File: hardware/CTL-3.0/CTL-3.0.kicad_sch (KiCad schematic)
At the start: 63 parts, among them J1 Conn_02x16_Top_Bottom, J2 Conn_02x05_Odd_Even, J3 Conn_01x03, J4 Conn_01x02, J5 Conn_02x06_Odd_Even, J6 Conn_01x04, J7 Conn_01x04, J8 Conn_01x04, K1 G5V-1, Q1 BCX56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

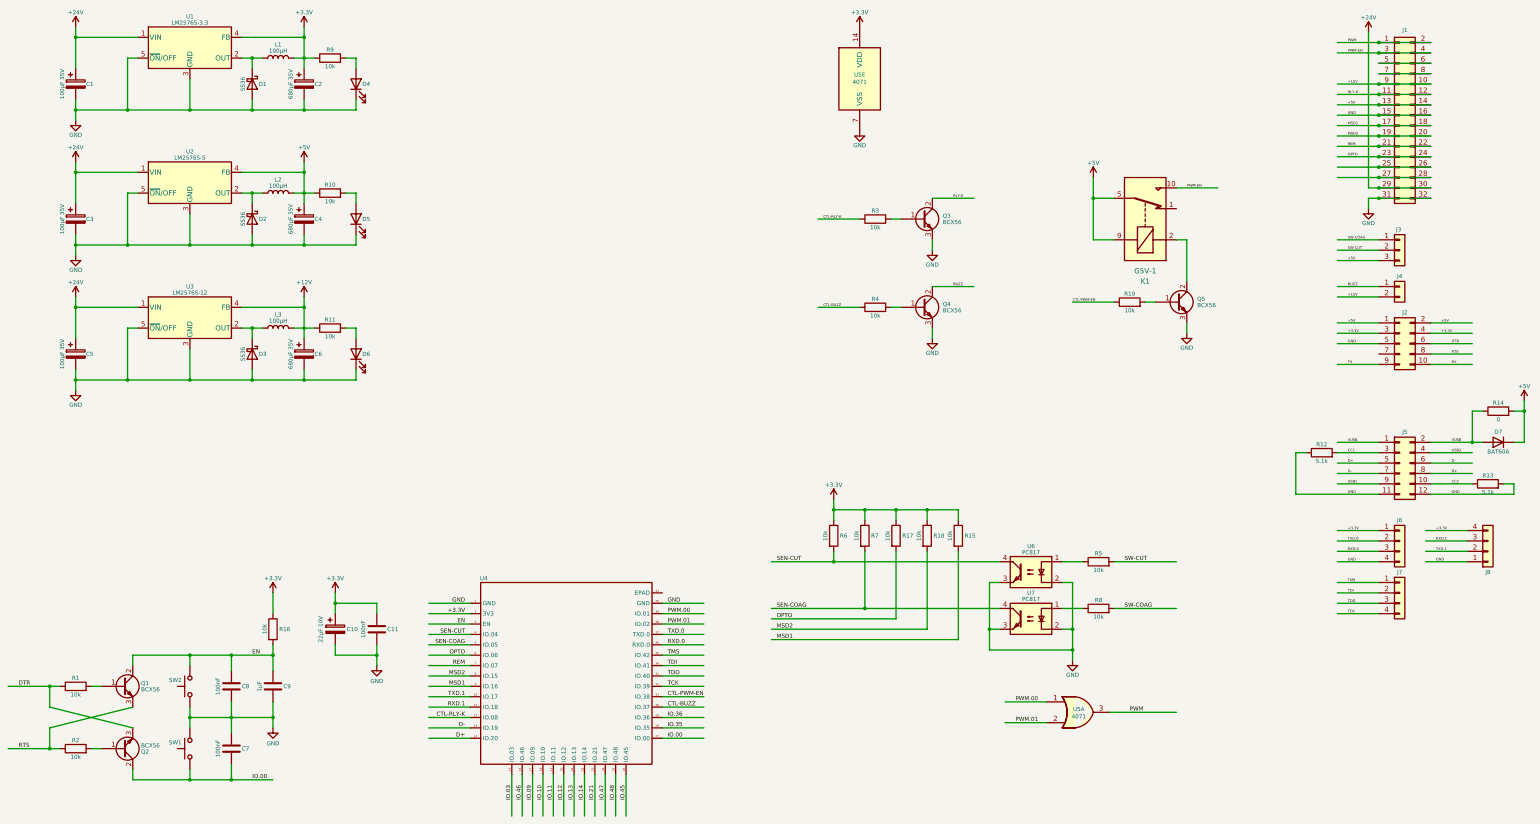
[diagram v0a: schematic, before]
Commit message: modified:   .DS_Store 	deleted:    hardware/CTL-2.0/CTL-1.0-backups/CTL-1.0-2025-06-05_145506.zip 	deleted:    hardware/CTL-2.0/CTL-1.0-backups/CTL-1.0-2025-06-10_100335.zip 	deleted:    hardware/CTL-2.0/CTL-1.0-backups/CTL-1.0-2025-06-12_095314.zip 	deleted:    hardware/CTL-2.0/CTL-1.0-backups/CTL-1.0-2025-07-03_115731.zip 	deleted:    hardware/CTL-2.0/CTL-1.0-backups/CTL-1.0-2025-07-16_143147.zip 	deleted:    hardware/CTL-2.0/CTL-1.0-backups/CTL-1.0-2025-07-24_151142.zip 	deleted:    hardware/CTL-2.0/CTL-1.0-backups/CTL-1.0-2025-07-24_172002.zip 	deleted:    hardware/CTL-2.0/CTL-1.0-backups/CTL-1.0-2025-07-25_175122.zip 	deleted:    hardware/CTL-2.0/CTL-1.0-backups/CTL-1.0-2025-07-26_120011.zip 	deleted:    hardware/CTL-2.0/CTL-1.0-backups/CTL-1.0-2025-07-26_120808.zip 	deleted:    hardware/CTL-2.0/CTL-1.0-backups/CTL-1.0-2025-07-28_094555.zip 	deleted:    hardware/CTL-2.0/CTL-1.0-backups/CTL-1.0-2025-07-28_104747.zip 	deleted:    hardware/CTL-2.0/CTL-1.0-backups/CTL-1.0-2025-07-28_112613.zip 	deleted:    hardware/CTL-2.0/CTL-1.0-backups/CTL-1.0-2025-07-28_114906.zip 	deleted:    hardware/CTL-2.0/CTL-1.0-backups/CTL-1.0-2025-07-28_120848.zip 	deleted:    hardware/CTL-2.0/CTL-1.0-backups/CTL-1.0-2025-07-29_085804.zip 	deleted:    hardware/CTL-2.0/CTL-1.0-backups/CTL-1.0-2025-07-29_150437.zip 	deleted:    hardware/CTL-2.0/CTL-1.0-backups/CTL-1.0-2025-07-30_093152.zip 	deleted:    hardware/CTL-2.0/CTL-1.0-backups/CTL-1.0-2025-07-31_095618.zip 	deleted:    hardware/CTL-2.0/CTL-1.0-backups/CTL-1.0-2025-08-01_111317.zip 	deleted:    hardware/CTL-2.0/CTL-1.0-backups/CTL-1.0-2025-08-01_113544.zip 	deleted:    hardware/CTL-2.0/CTL-1.0-backups/CTL-1.0-2025-08-01_114559.zip 	deleted:    hardware/CTL-2.0/CTL-1.0-backups/CTL-1.0-2025-08-01_115359.zip 	deleted:    hardware/CTL-2.0/CTL-1.0-backups/CTL-1.0-2025-08-01_115915.zip 	deleted:    hardware/CTL-2.0/CTL-1.0-backups/CTL-1.0-2025-08-01_131607.zip 	deleted:    hardware/CTL-2.0/CTL-1.2-TopSilkscreen.png 	deleted:    hardware/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
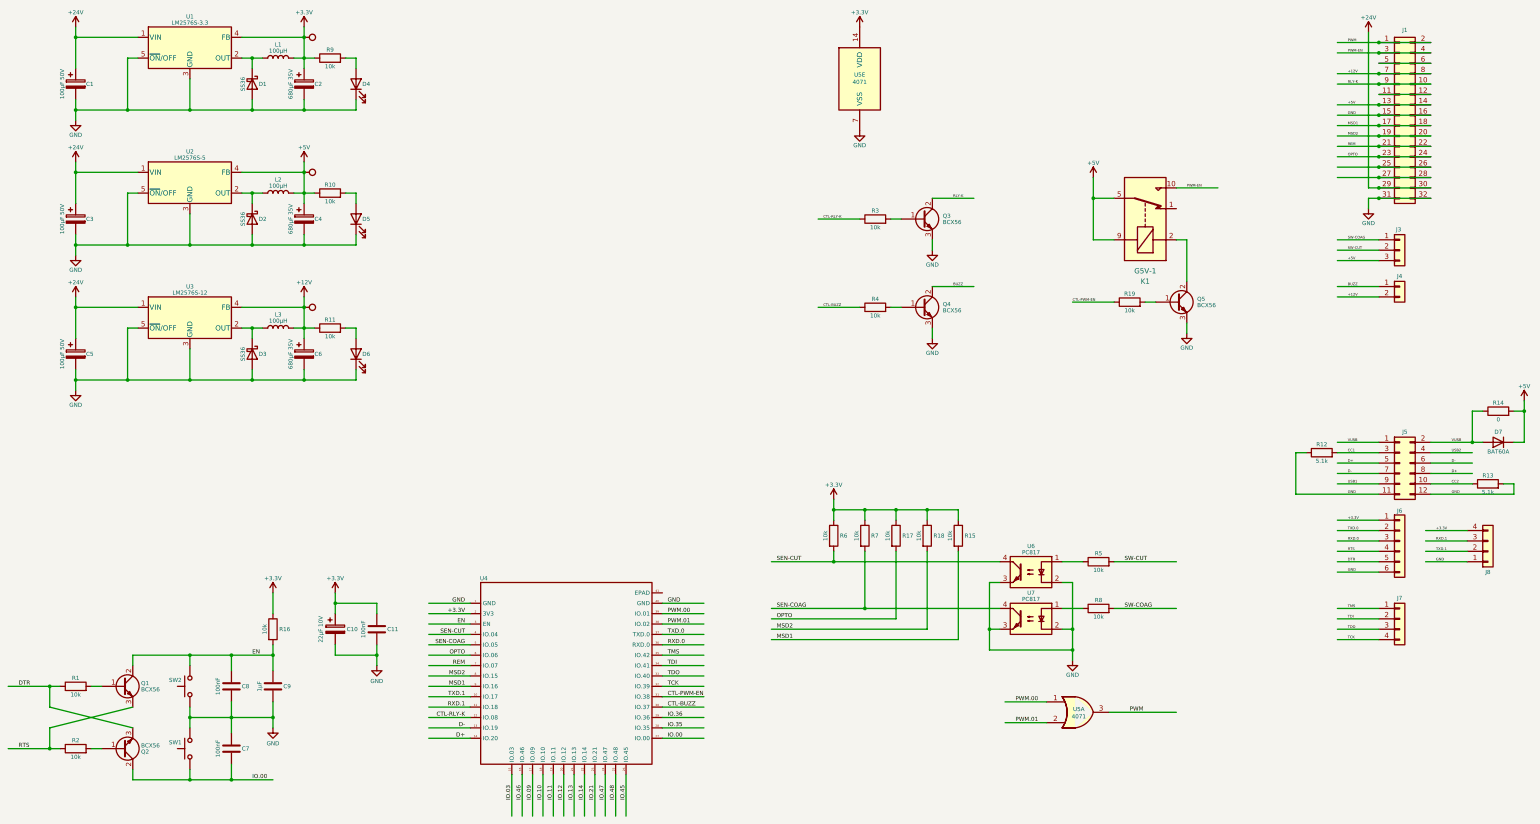
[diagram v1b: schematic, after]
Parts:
- removed J2: Conn_02x05_Odd_Even, Connector_PinHeader_2.54mm:PinHeader_2x05_P2.54mm_Vertical, symbol Connector_Generic:Conn_02x05_Odd_Even
- added TP1, TP2, TP3: TestPoint, TestPoint:TestPoint_Bridge_Pitch2.54mm_Drill1.0mm, symbol Connector:TestPoint
- C1, C3, C5: value 100µF 35V -> 100µF 50V
- J6: footprint Connector_PinHeader_2.54mm:PinHeader_1x04_P2.54mm_Vertical -> Connector_PinHeader_2.54mm:PinHeader_1x06_P2.54mm_Vertical; symbol Connector_Generic:Conn_01x04 -> Connector_Generic:Conn_01x06
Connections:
- net +12V: now also J1.7 (Pin_7), J1.8 (Pin_8), TP3.1; no longer J1.10 (Pin_10), J1.9 (Pin_9)
- net +3.3V: now also TP1.1
- net +5V: now also TP2.1
- net DTR: now also J6.5 (Pin_5)
- net GND: now also J6.6 (Pin_6); no longer J6.4 (Pin_4)
- net RLY-K: now also J1.10 (Pin_10), J1.9 (Pin_9); no longer J1.11 (Pin_11), J1.12 (Pin_12)
- net RTS: now also J6.4 (Pin_4)
- new net: J1.11 (Pin_11), J1.12 (Pin_12)
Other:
- moved on the sheet: J7

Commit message: modified:   .DS_Store 	modified:   README.md 	new file:   hardware/CTL-3.0/CTL-3.0-backups/CTL-3.0-2025-08-08_093936.zip 	new file:   hardware/CTL-3.0/CTL-3.0-backups/CTL-3.0-2025-08-08_103359.zip 	new file:   hardware/CTL-3.0/CTL-3.0-backups/CTL-3.0-2025-08-08_104842.zip 	new file:   hardware/CTL-3.0/CTL-3.0-backups/CTL-3.0-2025-08-08_105743.zip 	modified:   hardware/CTL-3.0/CTL-3.0.kicad_pcb 	modified:   hardware/CTL-3.0/CTL-3.0.kicad_sch 	modified:   hardware/CTL-3.0/CTL-3.0.step 	modified:   hardware/CTL-3.0/fp-info-cache 	modified:   hardware/MSD-1.0/MSD-1.0.step 	deleted:    hardware/PS-2.0/PS-2.0-backups/PS-2.0-2025-07-28_091511.zip 	deleted:    hardware/PS-2.0/PS-2.0-backups/PS-2.0-2025-07-28_120953.zip 	deleted:    hardware/PS-2.0/PS-2.0-backups/PS-2.0-2025-07-29_151613.zip 	deleted:    hardware/PS-2.0/PS-2.0-backups/PS-2.0-2025-07-30_104542.zip 	deleted:    hardware/PS-2.0/PS-2.0-backups/PS-2.0-2025-08-07_142024.zip 	new file:   hardware/PS-2.0/PS-2.0-backups/PS-2.0-2025-08-08_083444.zip 	new file:   hardware/PS-2.0/PS-2.0-backups/PS-2.0-2025-08-08_093021.zip 	new file:   hardware/PS-2.0/PS-2.0-backups/PS-2.0-2025-08-08_095017.zip 	new file:   hardware/PS-2.0/PS-2.0-backups/PS-2.0-2025-08-08_101231.zip 	new file:   hardware/PS-2.0/PS-2.0-backups/PS-2.0-2025-08-08_102520.zip 	modified:   hardware/PS-2.0/PS-2.0.kicad_pcb 	modified:   hardware/PS-2.0/PS-2.0.kicad_prl 	new file:   hardware/PS-2.0/~PS-2.0.kicad_pcb.lck 	modified:   hardware/REM-4.0/REM-4.0.step 	deleted:    hardware/XF-1.0/XF-1.0-backups/XF-1.0-2025-07-17_151907.zip 	deleted:    hardware/XF-1.0/XF-1.0-backups/XF-1.0-2025-08-07_145812.zip 	new file:   hardware/XF-1.0/XF-1.0-backups/XF-1.0-2025-08-08_083643.zip 	new file:   hardware/XF-1.0/XF-1.0-backups/XF-1.0-2025-08-08_100854.zip 	new file:   hardware/XF-1.0/XF-1.0-backups/XF-1.0-2025-08-08_101915.zip 	modified:   hardware/XF-1.0/XF-1.0.kicad_pcb 	modified:   hardware/XF-1.0/XF-1.0.step 	modified:   hardware/XF-1.0/fp-info-cache 	modified:   l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
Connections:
- net +12V: now also J4.1 (Pin_1); no longer J4.2 (Pin_2)
- net +5V: now also J3.1 (Pin_1); no longer J3.3 (Pin_3)
- net BUZZ: now also J4.2 (Pin_2); no longer J4.1 (Pin_1)
- net SW-COAG: now also J3.3 (Pin_3); no longer J3.1 (Pin_1)
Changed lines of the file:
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@@
 	(wire
 		(pts
-			(xy 351.79 72.39) (xy 361.95 72.39)
+			(xy 351.79 77.47) (xy 361.95 77.47)
 		)
 		(stroke
@@
 	(wire
 		(pts
-			(xy 351.79 77.47) (xy 361.95 77.47)
+			(xy 351.79 72.39) (xy 361.95 72.39)
 		)
 		(stroke
@@
 	(wire
 		(pts
-			(xy 351.79 83.82) (xy 361.95 83.82)
+			(xy 351.79 86.36) (xy 361.95 86.36)
 		)
 		(stroke
@@
 	(wire
 		(pts
-			(xy 351.79 86.36) (xy 361.95 86.36)
+			(xy 351.79 83.82) (xy 361.95 83.82)
 		)
 		(stroke
@@
 	)
 	(label "+5V"
-		(at 354.33 77.47 0)
+		(at 354.33 72.39 0)
 		(fields_autoplaced yes)
 		(effects
@@
 	)
 	(label "BUZZ"
-		(at 354.33 83.82 0)
+		(at 354.33 86.36 0)
 		(fields_autoplaced yes)
 		(effects
@@
 	)
 	(label "SW-COAG"
-		(at 354.33 72.39 0)
+		(at 354.33 77.47 0)
 		(fields_autoplaced yes)
 		(effects
@@
 	)
 	(label "+12V"
-		(at 354.33 86.36 0)
+		(at 354.33 83.82 0)
 		(fields_autoplaced yes)
 		(effects
@@
 	)
 	(symbol
+		(lib_id "Connector_Generic:Conn_01x03")
+		(at 367.03 74.93 0)
+		(unit 1)
+		(exclude_from_sim no)
+		(in_bom yes)
+		(on_board yes)
+		(dnp no)
+		(property "Reference" "J3"
+			(at 366.776 69.85 0)
+			(effects
+				(font
+					(size 1 1)
+				)
+			)
+		)
+		(property "Value" "Conn_01x03"
+			(at 369.57 76.1999 0)
+			(effects
+				(font
+					(size 1.27 1.27)
+				)
+				(justify left)
+				(hide yes)
+			)
+		)
+		(property "Footprint" "Connector_Molex:Molex_KK-396_5273-03A_1x03_P3.96mm_Vertical"
+			(at 367.03 74.93 0)
+			(effects
+				(font
+					(size 1.27 1.27)
+				)
+				(hide yes)
+			)
+		)
+		(property "Datasheet" "~"
+			(at 367.03 74.93 0)
+			(effects
+				(font
+					(size 1.27 1.27)
+				)
+				(hide yes)
+			)
+		)
+		(property "Description" "Generic connector, single row, 01x03, script generated (kicad-library-utils/schlib/autogen/connector/)"
+			(at 367.03 74.93 0)
+			(effects
+				(font
+					(size 1.27 1.27)
+				)
+				(hide yes)
+			)
+		)
+		(pin "1"
+		)
+		(pin "3"
+		)
+		(pin "2"
+		)
+		(instances
+			(project "CTL-3.0"
+				(path "/6b19d318-fbab-46b0-b882-d3538e8b12f1"
+					(reference "J3")
+					(unit 1)
+				)
+			)
+		)
+	)
+	(symbol
 		(lib_id "ESP32:ESP32-S3-WROOM-1U")
 		(at 139.7 161.29 0)
@@
 	)
 	(symbol
+		(lib_id "Connector_Generic:Conn_01x02")
+		(at 367.03 83.82 0)
+		(unit 1)
+		(exclude_from_sim no)
+		(in_bom yes)
+		(on_board yes)
+		(dnp no)
+		(property "Reference" "J4"
+			(at 367.03 81.28 0)
+			(effects
+				(font
+					(size 1 1)
+				)
+			)
+		)
+		(property "Value" "Conn_01x02"
+			(at 369.57 86.3599 0)
+			(effects
+				(font
+					(size 1.27 1.27)
+				)
+				(justify left)
+				(hide yes)
+			)
+		)
+		(property "Footprint" "Connector_Molex:Molex_KK-396_5273-02A_1x02_P3.96mm_Vertical"
+			(at 367.03 83.82 0)
+			(effects
+				(font
+					(size 1.27 1.27)
+				)
+				(hide yes)
+			)
+		)
+		(property "Datasheet" "~"
+			(at 367.03 83.82 0)
+			(effects
+				(font
+					(size 1.27 1.27)
+				)
+				(hide yes)
+			)
+		)
+		(property "Description" "Generic connector, single row, 01x02, script generated (kicad-library-utils/schlib/autogen/connector/)"
+			(at 367.03 83.82 0)
+			(effects
+				(font
+					(size 1.27 1.27)
+				)
+				(hide yes)
+			)
+		)
+		(pin "2"
+		)
+		(pin "1"
+		)
+		(instances
+			(project "CTL-3.0"
+				(path "/6b19d318-fbab-46b0-b882-d3538e8b12f1"
+					(reference "J4")
+					(unit 1)
+				)
+			)
+		)
+	)
+	(symbol
 		(lib_id "Device:R")
 		(at 391.16 114.3 90)
@@
 	)
 	(symbol
-		(lib_id "Connector_Generic:Conn_01x03")
-		(at 367.03 74.93 0)
-		(unit 1)
-		(exclude_from_sim no)
-		(in_bom yes)
-		(on_board yes)
-		(dnp no)
-		(property "Reference" "J3"
-			(at 366.776 69.85 0)
-			(effects
-				(font
-					(size 1 1)
-				)
-			)
-		)
-		(property "Value" "Conn_01x03"
-			(at 369.57 76.1999 0)
-			(effects
-				(font
-					(size 1.27 1.27)
-				)
-				(justify left)
-				(hide yes)
-			)
-		)
-		(property "Footprint" "Connector_Molex:Molex_KK-396_5273-03A_1x03_P3.96mm_Vertical"
-			(at 367.03 74.93 0)
-			(effects
-				(font
-					(size 1.27 1.27)
-				)
-				(hide yes)
-			)
-		)
-		(property "Datasheet" "~"
-			(at 367.03 74.93 0)
-			(effects
-				(font
-					(size 1.27 1.27)
-				)
-				(hide yes)
-			)
-		)
-		(property "Description" "Generic connector, single row, 01x03, script generated (kicad-library-utils/schlib/autogen/connector/)"
-			(at 367.03 74.93 0)
-			(effects
-				(font
-					(size 1.27 1.27)
-				)
-				(hide yes)
-			)
-		)
-		(pin "1"
-		)
-		(pin "3"
-		)
-		(pin "2"
-		)
-		(instances
-			(project ""
-				(path "/6b19d318-fbab-46b0-b882-d3538e8b12f1"
-					(reference "J3")
-					(unit 1)
-				)
-			)
-		)
-	)
-	(symbol
 		(lib_id "Connector_Generic:Conn_02x16_Odd_Even")
 		(at 367.03 41.91 0)
@@
 					(unit 1)
 				)
-			)
-		)
-	)
-	(symbol
-		(lib_id "Connector_Generic:Conn_01x02")
-		(at 367.03 83.82 0)
-		(unit 1)
-		(exclude_from_sim no)
-		(in_bom yes)
-		(on_board yes)
-		(dnp no)
-		(property "Reference" "J4"
-			(at 367.03 81.28 0)
-			(effects
-				(font
-					(size 1 1)
-				)
-			)
-		)
-		(property "Value" "Conn_01x02"
-			(at 369.57 86.3599 0)
-			(effects
-				(font
-					(size 1.27 1.27)
-				)
-				(justify left)
-				(hide yes)
-			)
-		)
-		(property "Footprint" "Connector_Molex:Molex_KK-396_5273-02A_1x02_P3.96mm_Vertical"
-			(at 367.03 83.82 0)
-			(effects
-				(font
-					(size 1.27 1.27)
-				)
-				(hide yes)
-			)
-		)
-		(property "Datasheet" "~"
-			(at 367.03 83.82 0)
-			(effects
-				(font
-					(size 1.27 1.27)
-				)
-				(hide yes)
-			)
-		)
-		(property "Description" "Generic connector, single row, 01x02, script generated (kicad-library-utils/schlib/autogen/connector/)"
-			(at 367.03 83.82 0)
-			(effects
-				(font
-					(size 1.27 1.27)
-				)
-				(hide yes)
-			)
-		)
-		(pin "2"
-		)
-		(pin "1"
-		)
-		(instances
-			(project ""
-				(path "/6b19d318-fbab-46b0-b882-d3538e8b12f1"
-					(reference "J4")
-					(unit 1)
-				)
